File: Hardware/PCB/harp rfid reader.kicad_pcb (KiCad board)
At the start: 4 copper layers, 45 x 26.5 mm, 65 parts, among them IC1 FT232RL, IC10 SN74LVC1G125DBVT, IC2 NJM11100F1-TE2, IC3 ATxmega32A4U-A, IC4 SN74LVC1G125DBVT, IC5 SN74LVC1G125DBVT, J1 USB4105-GF-A, J2 282834-2, J3 NPPN051BFLD-RC, J4 NPPN071BFLC-RC, Q1 BC817-40W, Q2 NTF2955T1G, U2 TPD4E05U06DQA, X1 O 32,0-JT32C-A-K-3,3-LF

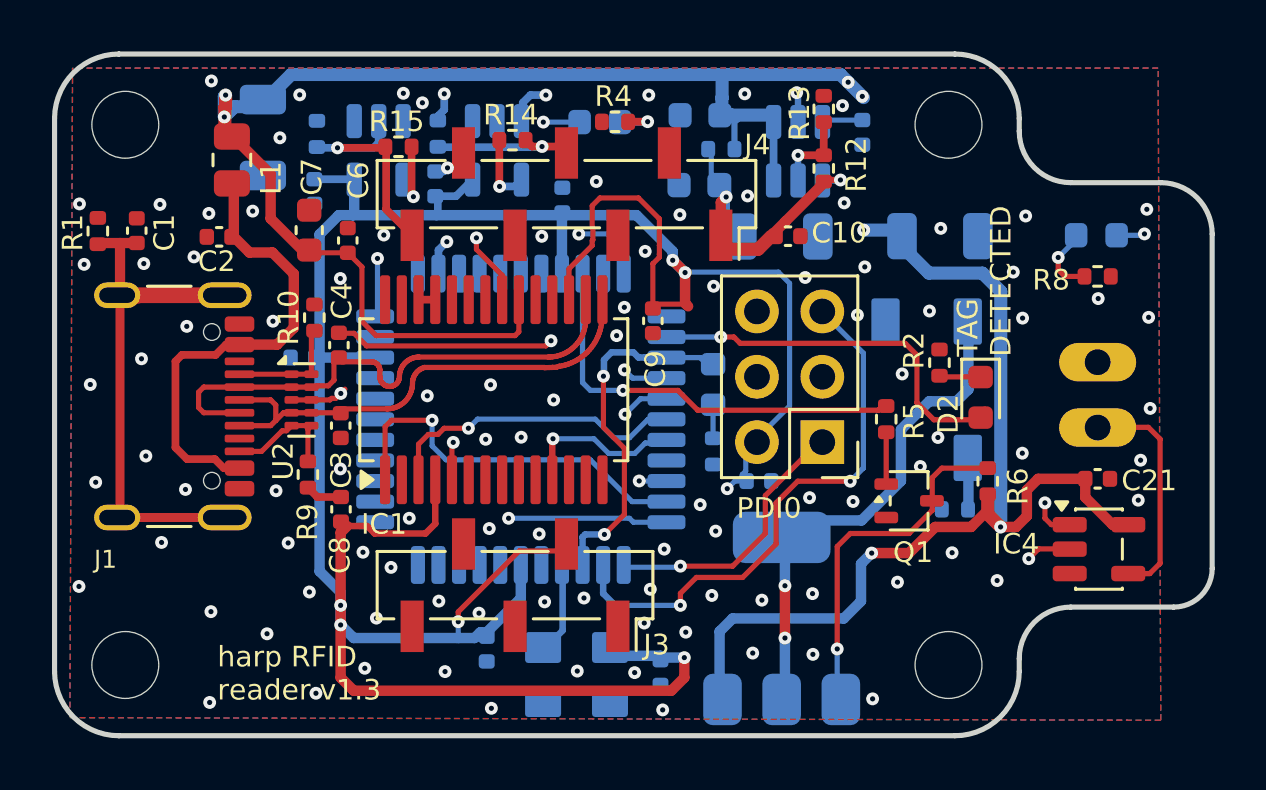
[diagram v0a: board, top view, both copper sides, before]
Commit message: MPN de IC4 IC5 IC10 não estavam correctos
. corrigidos MPN & footprints
. rerouting feito: DRC=0
. gerados ficheiros produção
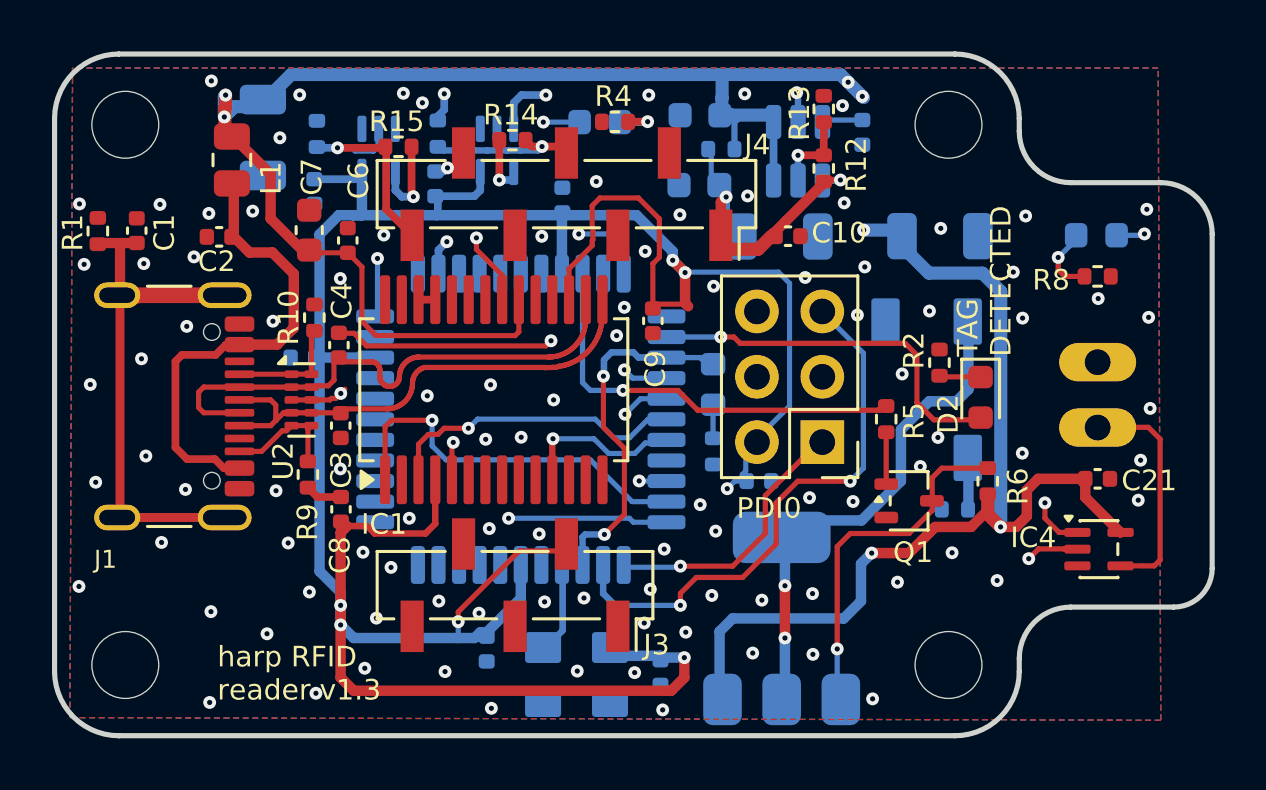
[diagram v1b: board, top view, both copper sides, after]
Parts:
- IC10, IC4, IC5: value SN74LVC1G125DBVT -> MC74VHC1GT125DBVT1G; footprint Package_TO_SOT_SMD:SOT-23-5 -> Package_TO_SOT_SMD:SOT-353_SC-70-5
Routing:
- net +3V3: track 117.7 -> 119.5 mm
- net GND: track 21.8 -> 22.8 mm
- net /core/UC_F2: track 7.06 -> 7.74 mm
- net Net-(J2-Pin_1): track 9.58 -> 8.96 mm
- net /core/UC_TX: track 10.5 -> 9.99 mm

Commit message: dorrecção em ligação módulo RFID
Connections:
- J3 pad 2: +3V3 -> VRFID
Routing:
- net VRFID: track 13.1 -> 33.4 mm, vias 2 -> 3
- net +3V3: track 119.5 -> 112.9 mm, vias 8 -> 7
- net GND: vias 104 -> 103
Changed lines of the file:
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@@
 			(size 2 0.9)
 			(layers "F.Cu" "F.Mask" "F.Paste")
-			(net "+3V3")
+			(net "VRFID")
 			(pinfunction "Pin_2_2")
 			(pintype "passive")
@@
 		(tags "resistor")
 		(property "Reference" "R3"
-			(at -0.87 -0.38 270)
+			(at -0.850799 -0.38 270)
 			(layer "B.SilkS")
 			(effects
@@
 	)
 	(via
-		(at 151.17 78.430801)
+		(at 150.9 78.430801)
 		(size 0.5)
 		(drill 0.2)
@@
 	)
 	(via
-		(at 151.25 87.949201)
-		(size 0.5)
-		(drill 0.2)
-		(layers "F.Cu" "B.Cu")
-		(net "GND")
-	)
-	(via
 		(at 127.15 86.049201)
 		(size 0.5)
@@
 	)
 	(via
-		(at 150.65 86.919201)
+		(at 151.049701 87.301171)
 		(size 0.5)
 		(drill 0.2)
@@
 	)
 	(segment
+		(start 147.621799 88.678201)
+		(end 145.679 88.678201)
+		(width 0.3)
+		(layer "F.Cu")
+		(net "VRFID")
+	)
+	(segment
+		(start 145.679 88.678201)
+		(end 145.45 88.449201)
+		(width 0.3)
+		(layer "F.Cu")
+		(net "VRFID")
+	)
+	(segment
+		(start 145.4655 88.465401)
+		(end 145.2115 88.719401)
+		(width 0.2032)
+		(layer "F.Cu")
+		(net "VRFID")
+	)
+	(segment
+		(start 150.9 88)
+		(end 148.3 88)
+		(width 0.3)
+		(layer "F.Cu")
+		(net "VRFID")
+	)
+	(segment
 		(start 153.4121 76.460801)
 		(end 153.4121 76.483801)
@@
 	)
 	(segment
+		(start 148.3 88)
+		(end 147.621799 88.678201)
+		(width 0.3)
+		(layer "F.Cu")
+		(net "VRFID")
+	)
+	(segment
 		(start 155.45 74.422901)
 		(end 155.45 74.359201)
@@
 	)
 	(via
+		(at 150.9 88)
+		(size 0.5)
+		(drill 0.2)
+		(layers "F.Cu" "B.Cu")
+		(free yes)
+		(net "VRFID")
+	)
+	(via
 		(at 151.6571 74.959801)
 		(size 0.5)
@@
 	)
 	(segment
+		(start 150.05 87.16773)
+		(end 150.401471 87.519201)
+		(width 0.3)
+		(layer "In2.Cu")
+		(net "VRFID")
+	)
+	(segment
+		(start 151.6571 74.959801)
+		(end 151.6571 78.79223)
+		(width 0.3)
+		(layer "In2.Cu")
+		(net "VRFID")
+	)
+	(segment
+		(start 150.401471 87.519201)
+		(end 150.419201 87.519201)
+		(width 0.3)
+		(layer "In2.Cu")
+		(net "VRFID")
+	)
+	(segment
+		(start 150 87.1)
+		(end 150.05 87.15)
+		(width 0.3)
+		(layer "In2.Cu")
+		(net "VRFID")
+	)
+	(segment
+		(start 150.419201 87.519201)
+		(end 150.9 88)
+		(width 0.3)
+		(layer "In2.Cu")
+		(net "VRFID")
+	)
+	(segment
+		(start 151.6571 78.79223)
+		(end 150 80.44933)
+		(width 0.3)
+		(layer "In2.Cu")
+		(net "VRFID")
+	)
+	(segment
+		(start 150 80.44933)
+		(end 150 87.1)
+		(width 0.3)
+		(layer "In2.Cu")
+		(net "VRFID")
+	)
+	(segment
+		(start 150.05 87.15)
+		(end 150.05 87.16773)
+		(width 0.3)
+		(layer "In2.Cu")
+		(net "VRFID")
+	)
+	(segment
 		(start 150.5525 83.249201)
 		(end 149.7815 82.478201)
@@
 	)
 	(segment
-		(start 145.2115 88.719401)
-		(end 143.6125 88.719401)
-		(width 0.2032)
-		(layer "F.Cu")
-		(net "+3V3")
-	)
-	(segment
 		(start 146.4783 76.627019)
 		(end 146.45 76.655319)
@@
 	)
 	(segment
-		(start 150.06 79.091101)
-		(end 150.1786 79.209701)
-		(width 0.4064)
-		(layer "F.Cu")
-		(net "+3V3")
-	)
-	(segment
 		(start 146.45 75.299201)
 		(end 146.45 76.143083)
@@
 	)
 	(segment
-		(start 145.4655 88.465401)
-		(end 145.2115 88.719401)
-		(width 0.2032)
-		(layer "F.Cu")
-		(net "+3V3")
-	)
-	(segment
 		(start 136.6711 91.596801)
 		(end 136.6711 90.834801)
@@
 	)
 	(segment
-		(start 150.1786 79.209701)
-		(end 150.0944 79.125501)
-		(width 0.2)
-		(layer "F.Cu")
-		(net "+3V3")
-	)
-	(segment
 		(start 146.4783 76.171383)
 		(end 146.4783 76.627019)
@@
 	)
 	(segment
-		(start 143.6125 88.719401)
-		(end 141.2431 91.088801)
-		(width 0.2032)
-		(layer "F.Cu")
-		(net "+3V3")
-	)
-	(segment
 		(start 148.8089 79.125501)
 		(end 148.8089 77.553661)
@@
 	)
 	(segment
-		(start 141.2431 91.088801)
-		(end 141.2431 91.469801)
-		(width 0.2032)
-		(layer "F.Cu")
-		(net "+3V3")
-	)
-	(segment
 		(start 136.6711 90.834801)
 		(end 136.6711 88.004901)
@@
 	)
 	(via
-		(at 141.2431 91.469801)
-		(size 0.5)
-		(drill 0.2)
-		(layers "F.Cu" "B.Cu")
-		(net "+3V3")
-	)
-	(via
 		(at 150.06 77.899201)
 		(size 0.5)
@@
 		(layer "B.Cu")
 		(net "+3V3")
-	)
-	(segment
-		(start 141.2431 91.469801)
-		(end 141.2431 92.104801)
-		(width 0.2032)
-		(layer "B.Cu")
-		(net "+3V3")
